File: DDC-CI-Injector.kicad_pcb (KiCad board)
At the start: 4 copper layers, 49.1 x 39.3 mm, 25 parts, among them J1 HDMI_A, J2 HDMI_A, J3 Connector, U1 PCA9641, U2 XC6206PxxxMR, U3 PCA9509, U4 PCA9509, U5 ESD224DQA, U6 ESD224DQA, U7 ESD224DQA

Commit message: Better routing
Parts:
- J2: moved to B.Cu
- moved R2 5.81 mm to (101.9, 60.5)
- moved C2 5.81 mm to (113.0, 69.2)
- moved C4 5.81 mm to (114.2, 65.5)
- moved R7 5.81 mm to (115.5, 59.8)
- moved U1 5.81 mm to (112.0, 60.5)
- moved U2 5.81 mm to (110.1, 69.5)
- moved U4 5.81 mm to (103.3, 63.0)
- moved C1 5.81 mm to (110.7, 72.0)
- moved C3 5.81 mm to (115.6, 66.0)
- moved R1 5.81 mm to (101.8, 55.5)
- moved R3 5.81 mm to (99.8, 64.0)
- moved R4 5.81 mm to (99.8, 62.0)
- moved R5 5.81 mm to (99.8, 57.0)
- moved U3 5.81 mm to (103.3, 58.0)
- moved R6 5.81 mm to (99.8, 59.0)
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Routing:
- net /D2_B-: track 47.9 -> 11.8 mm, vias 2 -> 1
- net /CK_B+: track 44.6 -> 10.5 mm, vias 0 -> 1
- net /D0_B+: track 44.7 -> 10.9 mm, vias 0 -> 1
- net /D1_B+: track 44.9 -> 11.2 mm, vias 0 -> 1
- net /D1_B-: track 44.8 -> 11.2 mm, vias 0 -> 1
- net /CK_B-: track 43.3 -> 10.5 mm, vias 0 -> 1
- net /D0_B-: track 43.4 -> 10.9 mm, vias 0 -> 1
- net /D2_B+: track 41.8 -> 11.8 mm, vias 2 -> 1
- net Net-(J1-HPD): track 30.9 -> 16.7 mm
- net Net-(J2-CEC): track 25.7 -> 12.3 mm, vias 2 -> 1
- net Net-(J2-UTILITY): track 25.4 -> 12.5 mm, vias 4 -> 1
- net GND: track 46.2 -> 38.3 mm, vias 26 -> 33
- net +3V3: track 47.0 -> 40.8 mm
- net Net-(J2-SCL): track 20.3 -> 15.1 mm, vias 2 -> 1
- net Net-(U3-B1): track 10.6 -> 14.8 mm
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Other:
- board size 49.1 x 39.3 mm -> 49.1 x 35.5 mm

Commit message: Fix small stuff
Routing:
- net GND: track 38.3 -> 42.8 mm, vias 33 -> 37
- net +5V: track 61.8 -> 62.6 mm

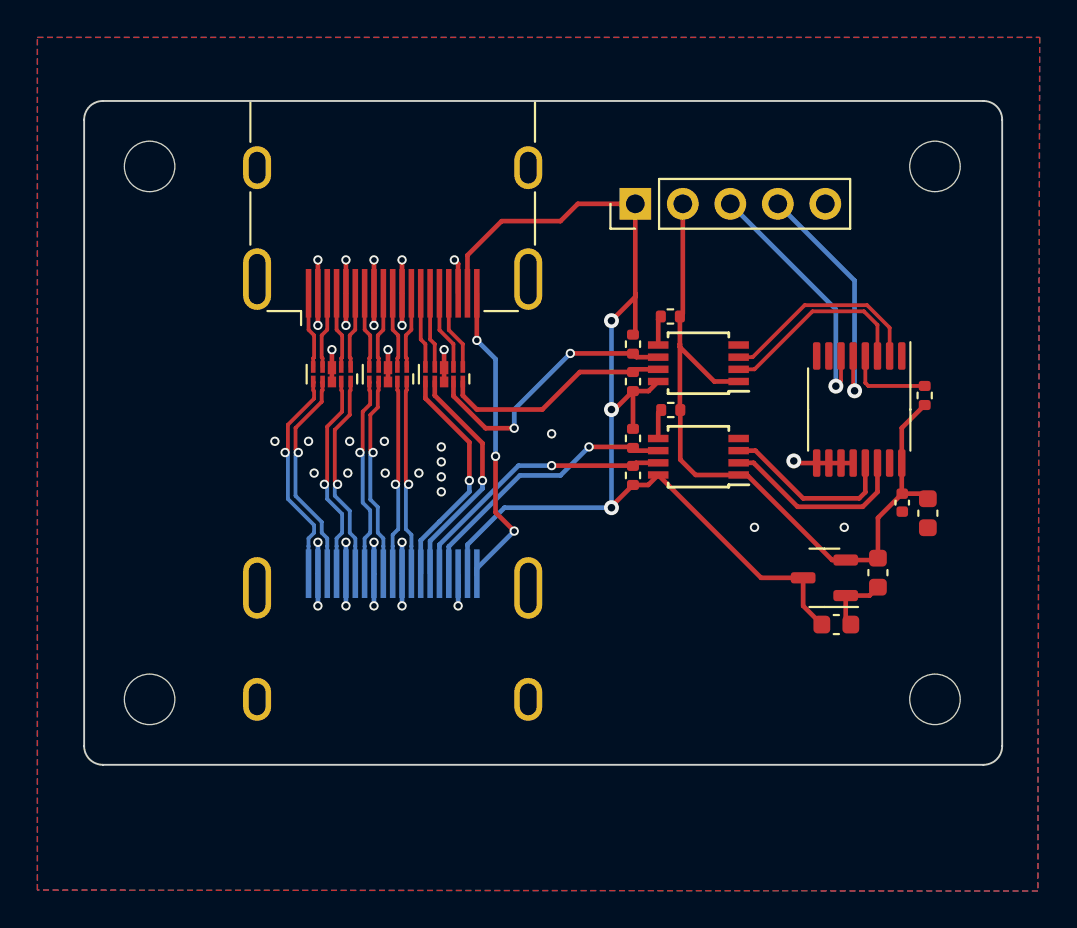
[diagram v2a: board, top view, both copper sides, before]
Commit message: Fix traces and other small stuff, add silkscreen
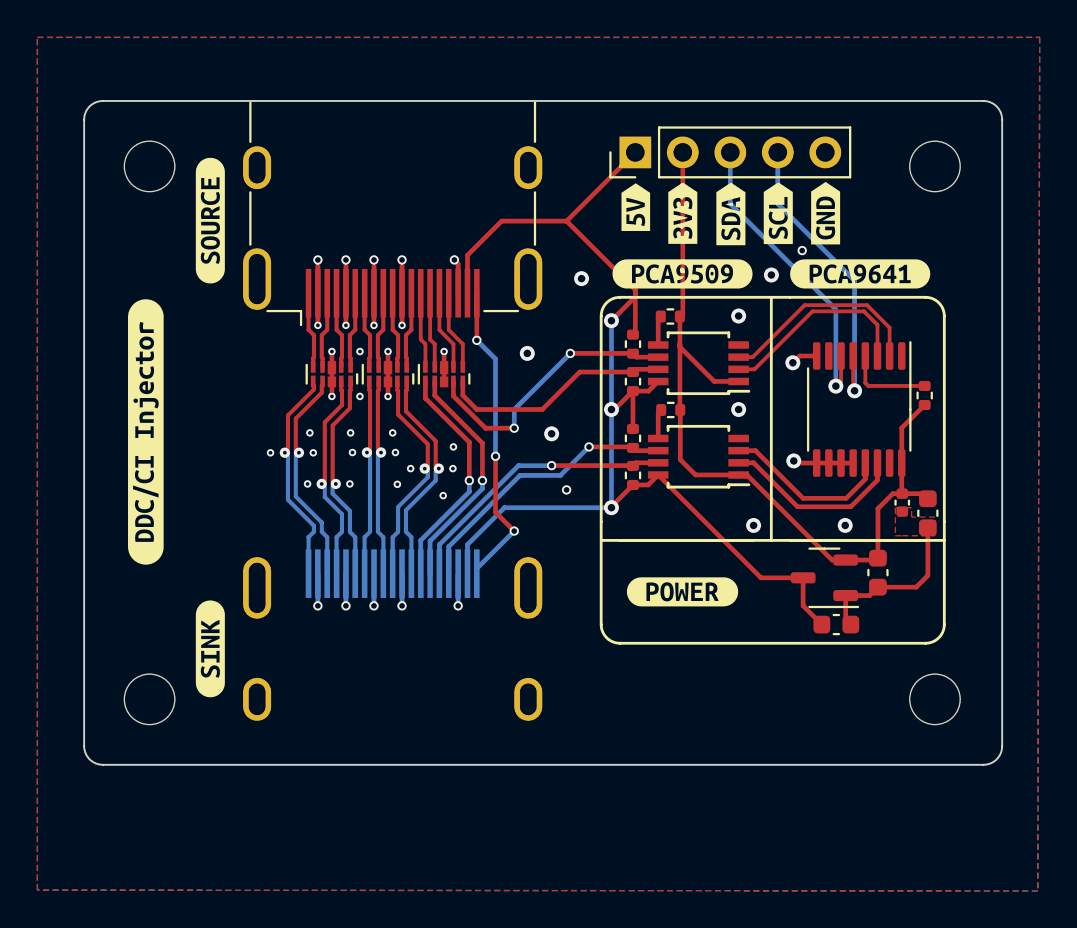
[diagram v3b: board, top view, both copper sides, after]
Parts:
- added kibuzzard-65C788DA: G***, kibuzzard-65C788DA, F.Cu at (77.2, 50.4)
- added kibuzzard-65C788DA: G***, kibuzzard-65C788DA, B.Cu at (77.2, 50.4)
- added kibuzzard-65C788F4: G***, kibuzzard-65C788F4, F.Cu at (77.2, 73.3)
- added kibuzzard-65C788F4: G***, kibuzzard-65C788F4, B.Cu at (77.2, 73.3)
- added kibuzzard-65C7895D: G***, kibuzzard-65C7895D, F.Cu at (112.0, 53.2)
- added kibuzzard-65C78967: G***, kibuzzard-65C78967, F.Cu at (102.5, 53.2)
- added kibuzzard-65C78A0C: G***, kibuzzard-65C78A0C, F.Cu at (102.5, 50.0)
- added kibuzzard-65C78A2B: G***, kibuzzard-65C78A2B, F.Cu at (105.1, 50.0)
- added kibuzzard-65C78A2F: G***, kibuzzard-65C78A2F, F.Cu at (107.6, 50.0)
- added kibuzzard-65C78A34: G***, kibuzzard-65C78A34, F.Cu at (110.2, 50.0)
- added kibuzzard-65C78A39: G***, kibuzzard-65C78A39, F.Cu at (100.0, 49.7)
- added kibuzzard-65C78A58: G***, kibuzzard-65C78A58, F.Cu at (102.5, 70.2)
- added kibuzzard-65C78CFB: G***, kibuzzard-65C78CFB, F.Cu at (73.8, 61.7)
- moved J3 2.75 mm to (100.0, 46.8)
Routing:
- net +3V3: track 40.8 -> 43.8 mm
- net Net-(J3-Pin_4): track 13.6 -> 16.3 mm
- net Net-(J3-Pin_3): track 13.8 -> 16.6 mm
- net +5V: track 62.6 -> 64.2 mm
- net GND: track 42.8 -> 44.2 mm, vias 37 -> 47
- net /CK_B+: track 10.8 -> 11.9 mm
- net /CK_B-: track 10.8 -> 11.9 mm
